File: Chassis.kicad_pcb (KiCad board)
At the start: 2 copper layers, 78.7 x 94.5 mm, 50 parts, among them IC1 RT6285GSP, IC2 LV2862YDDCR, J1 FR_JST, J10 BL_XT30, J11 Sabre Vertical Header 6, J12 Conn_01x12, J2 FR_XT30, J3 BR_JST, J4 BR_XT30, J5 IN_JST, J6 IN_XT60, J7 FL_JST, J8 FL_XT30, J9 BL_JST

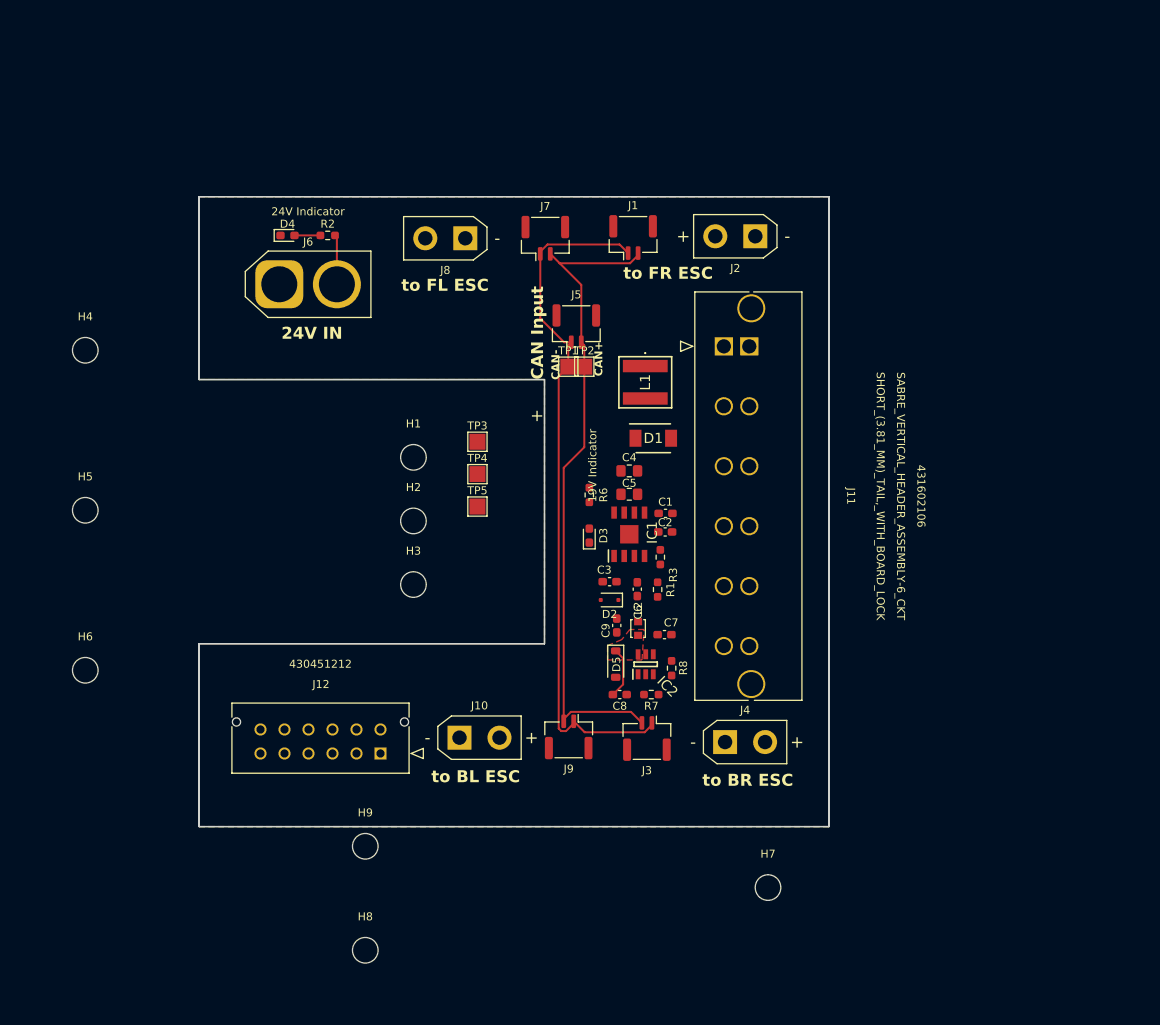
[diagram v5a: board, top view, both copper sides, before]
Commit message: attempted to wire buck converter
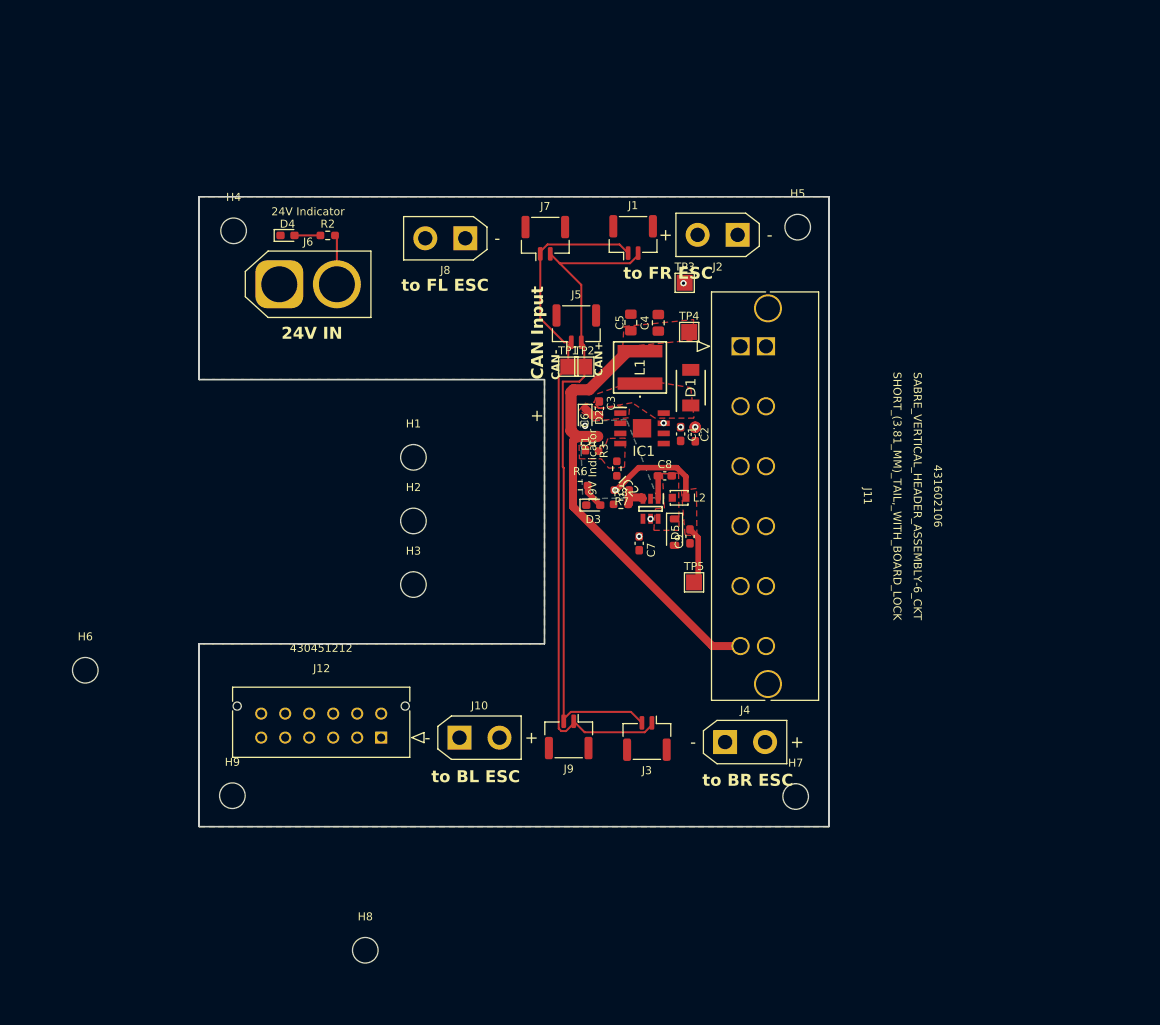
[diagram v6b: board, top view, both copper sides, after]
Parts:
- moved H5 95.8 mm to (184.0, 54.6)
- moved TP3 32.6 mm to (169.9, 61.6)
- moved TP4 31.9 mm to (170.5, 67.7)
- moved TP5 28.7 mm to (171.1, 99.0)
- moved C8 27.9 mm to (167.4, 85.7), turned to 0 degrees
- moved R7 25.8 mm to (162.1, 87.5)
- moved H4 23.8 mm to (113.5, 55.1)
- moved D2 23.1 mm to (157.5, 78.4), turned to -90 degrees
- moved C3 21.7 mm to (159.3, 77.3), turned to 90 degrees
- moved C5 21.5 mm to (163.2, 66.5), turned to 90 degrees
- moved R8 21.4 mm to (162.0, 89.3), turned to 180 degrees
- moved R1 19.7 mm to (159.2, 81.7), turned to -90 degrees
- moved IC2 19.4 mm to (165.7, 89.8), turned to -90 degrees
- moved C6 19.3 mm to (157.5, 81.6), turned to -90 degrees
- moved C4 18.9 mm to (166.6, 66.6), turned to 90 degrees
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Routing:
- net /V_{OUT}: track 0.00 -> 62.8 mm
- net +5V: track 0.00 -> 20.4 mm, vias 0 -> 2
- net /24V -> 19V Buck Convertor/SW_{5}: track 6.37 -> 0.00 mm
- net /24V -> 19V Buck Convertor/FB_{5}: track 0.00 -> 3.61 mm
- net Net-(D3-A): track 0.00 -> 3.10 mm
- net /24V -> 19V Buck Convertor/BOOT_{5}: track 0.00 -> 2.88 mm
- net /24V -> 19V Buck Convertor/BOOT_{19}: track 0.00 -> 2.13 mm
- net /CAN+: track 82.7 -> 84.0 mm
- net +24V: track 6.20 -> 6.31 mm, vias 0 -> 6
- added copper zone on B.Cu, net +5V
- added copper zone on F.Cu, net +5V
- added copper zone on F.Cu, net /24V -> 19V Buck Convertor/BOOT_{19}
- added copper zone on F.Cu, net /24V -> 19V Buck Convertor/FB_{19}
- added copper zone on F.Cu, net /24V -> 19V Buck Convertor/SW_{19}
- added copper zone on F.Cu, net /V_{OUT}

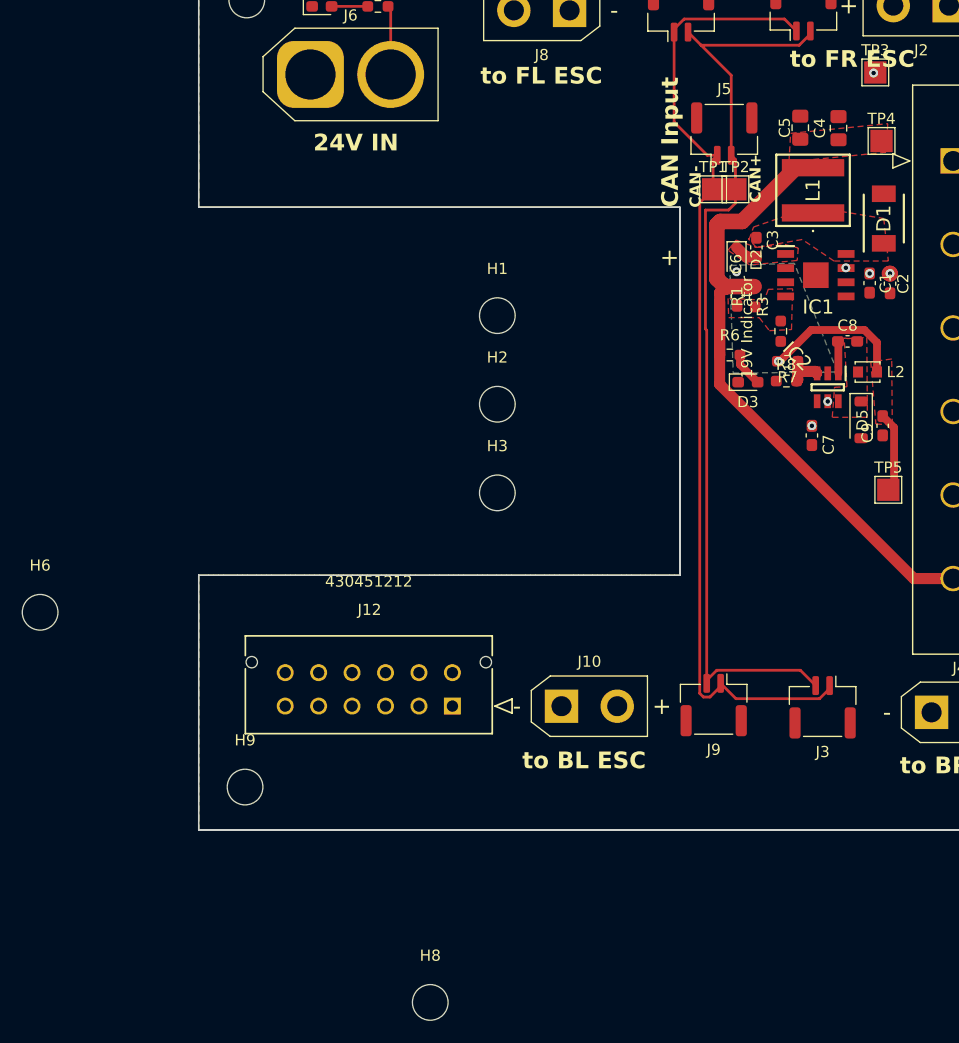
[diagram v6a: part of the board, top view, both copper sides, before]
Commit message: Remove unnecessary holes + made some thermal vias into direct pours
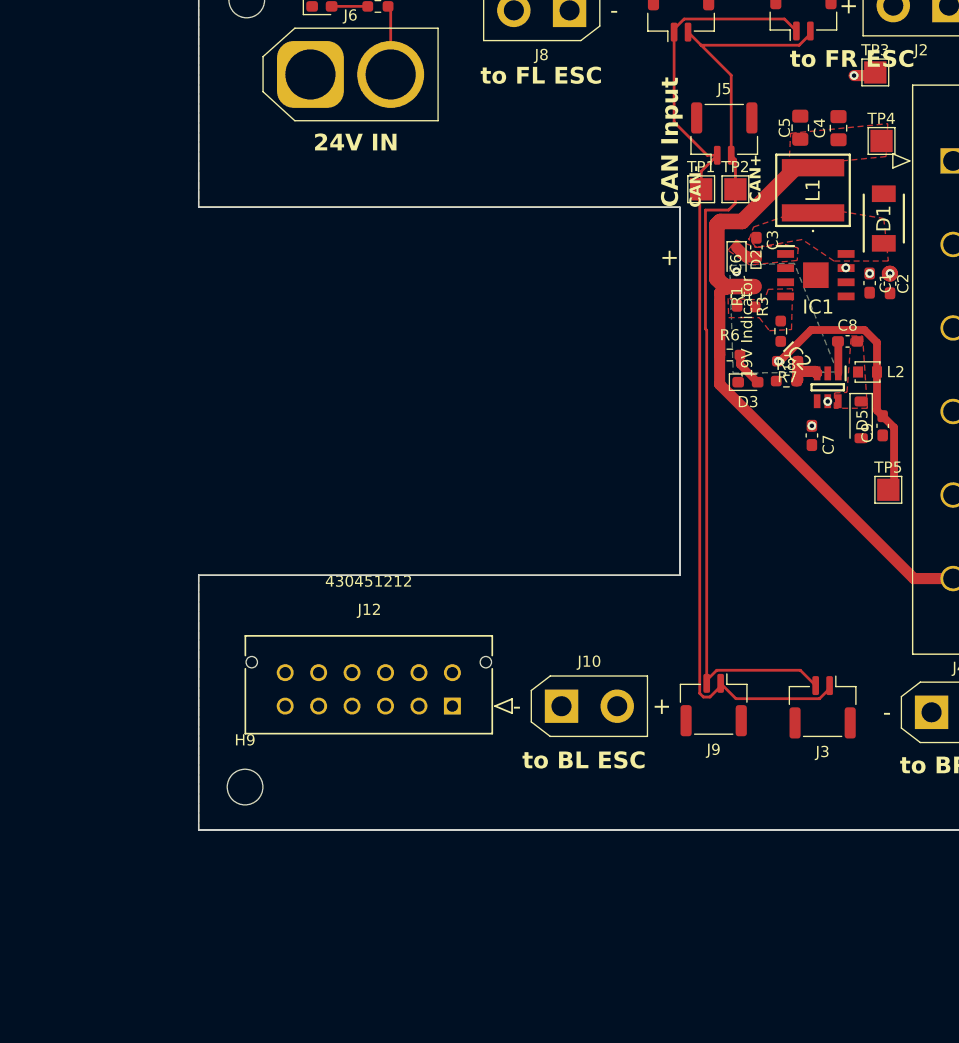
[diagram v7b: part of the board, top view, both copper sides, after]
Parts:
- removed H1, H2, H3, H6, H8: MountingHole, MountingHole:MountingHole_3.2mm_M3
- moved TP1 1.07 mm to (154.3, 72.0)
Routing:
- net +5V: track 20.4 -> 24.6 mm
- net +24V: track 6.31 -> 8.33 mm
- removed copper zone on F.Cu, net +5V

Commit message: Clear PCB
Rerouting hajimaruyo
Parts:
- removed C1, C2: 4.7µF, Capacitor_SMD:C_0603_1608Metric_Pad1.08x0.95mm_HandSolder
- removed C3: 10nF, Capacitor_SMD:C_0603_1608Metric_Pad1.08x0.95mm_HandSolder
- removed C4, C5: 22µF, Capacitor_SMD:C_0805_2012Metric_Pad1.18x1.45mm_HandSolder
- removed C6: 82pF, Capacitor_SMD:C_0603_1608Metric_Pad1.08x0.95mm_HandSolder
- removed C7: 2.2 μF, Capacitor_SMD:C_0603_1608Metric_Pad1.08x0.95mm_HandSolder
- removed C8: 100 nF, Capacitor_SMD:C_0603_1608Metric_Pad1.08x0.95mm_HandSolder
- removed C9: 10 nF, Capacitor_SMD:C_0603_1608Metric_Pad1.08x0.95mm_HandSolder
- removed D1: SR54F-AU_R2_000A1, Robomaster_ICs:SODFL5336X110N
- removed D2: BAS321J, Diode_SMD:D_SOD-323F
- removed D3: 150060BS75000, LED_SMD:LED_0603_1608Metric_Pad1.05x0.95mm_HandSolder
- removed D4: 150060RS75000, LED_SMD:LED_0603_1608Metric_Pad1.05x0.95mm_HandSolder
- removed D5: SD103AW-TP, Diode_SMD:D_SOD-123
- removed IC1: RT6285GSP, Robomaster_ICs:SOIC127P600X175-9N
- removed IC2: LV2862YDDCR, Robomaster_ICs:SOT95P280X110-6N
- removed J1: FR_JST, Connector_JST:JST_GH_BM02B-GHS-TBT_1x02-1MP_P1.25mm_Vertical
- removed J10: BL_XT30, Connector_AMASS:AMASS_XT30UPB-F_1x02_P5.0mm_Vertical
- removed J11: Sabre Vertical Header 6, Robomaster_ICs:CON_431602106_MOL
- removed J12: Conn_01x12, Robomaster_ICs:CON_430451212_MOL
- removed J2: FR_XT30, Connector_AMASS:AMASS_XT30UPB-F_1x02_P5.0mm_Vertical
- removed J3: BR_JST, Connector_JST:JST_GH_BM02B-GHS-TBT_1x02-1MP_P1.25mm_Vertical
- removed J4: BR_XT30, Connector_AMASS:AMASS_XT30UPB-F_1x02_P5.0mm_Vertical
- removed J5: IN_JST, Connector_JST:JST_GH_BM02B-GHS-TBT_1x02-1MP_P1.25mm_Vertical
- removed J6: IN_XT60, Connector_AMASS:AMASS_XT60-F_1x02_P7.20mm_Vertical
- removed J7: FL_JST, Connector_JST:JST_GH_BM02B-GHS-TBT_1x02-1MP_P1.25mm_Vertical
- removed J8: FL_XT30, Connector_AMASS:AMASS_XT30UPB-F_1x02_P5.0mm_Vertical
- removed J9: BL_JST, Connector_JST:JST_GH_BM02B-GHS-TBT_1x02-1MP_P1.25mm_Vertical
- removed L1: 10µH, Robomaster_ICs:MPLAL6060100
- removed L2: 33 μH, Inductor_SMD:L_Murata_LQH2MCNxxxx02_2.0x1.6mm
- removed R1: 100kΩ, Resistor_SMD:R_0603_1608Metric_Pad0.98x0.95mm_HandSolder
- removed R2: 1kΩ, Resistor_SMD:R_0603_1608Metric_Pad0.98x0.95mm_HandSolder
- removed R3: 6.8kΩ, Resistor_SMD:R_0603_1608Metric_Pad0.98x0.95mm_HandSolder
- removed R6: 680Ω, Resistor_SMD:R_0603_1608Metric_Pad0.98x0.95mm_HandSolder
- removed R7: 56 kΩ, Resistor_SMD:R_0603_1608Metric_Pad0.98x0.95mm_HandSolder
- removed R8: 10 kΩ, Resistor_SMD:R_0603_1608Metric_Pad0.98x0.95mm_HandSolder
- removed TP1, TP2, TP3, TP4, TP5: TestPoint, TestPoint:TestPoint_Pad_2.0x2.0mm
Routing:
- net /CAN-: track 87.8 -> 0.00 mm
- net /CAN+: track 84.0 -> 0.00 mm
- net /V_{OUT}: track 62.8 -> 0.00 mm
- net +5V: track 24.6 -> 0.00 mm, vias 2 -> 0
- net +24V: track 8.33 -> 0.00 mm, vias 6 -> 0
- net /24V -> 19V Buck Convertor/FB_{5}: track 3.61 -> 0.00 mm
- net Net-(D4-A): track 3.24 -> 0.00 mm
- net Net-(D3-A): track 3.10 -> 0.00 mm
- net /24V -> 19V Buck Convertor/BOOT_{5}: track 2.88 -> 0.00 mm
- net /24V -> 19V Buck Convertor/BOOT_{19}: track 2.13 -> 0.00 mm
- removed copper zone on B.Cu, net +5V
- removed copper zone on F.Cu, net /24V -> 19V Buck Convertor/BOOT_{19}
- removed copper zone on F.Cu, net /24V -> 19V Buck Convertor/FB_{19}
- removed copper zone on F.Cu, net /24V -> 19V Buck Convertor/SW_{19}
- removed copper zone on F.Cu, net /24V -> 19V Buck Convertor/SW_{5}
- removed copper zone on F.Cu, net /V_{OUT}
